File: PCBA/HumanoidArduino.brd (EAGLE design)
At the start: 105.4 x 75.2 mm, 8 parts, among them J1 22-27-2061-06, J2 22-27-2041-04, J3 22-27-2031-03

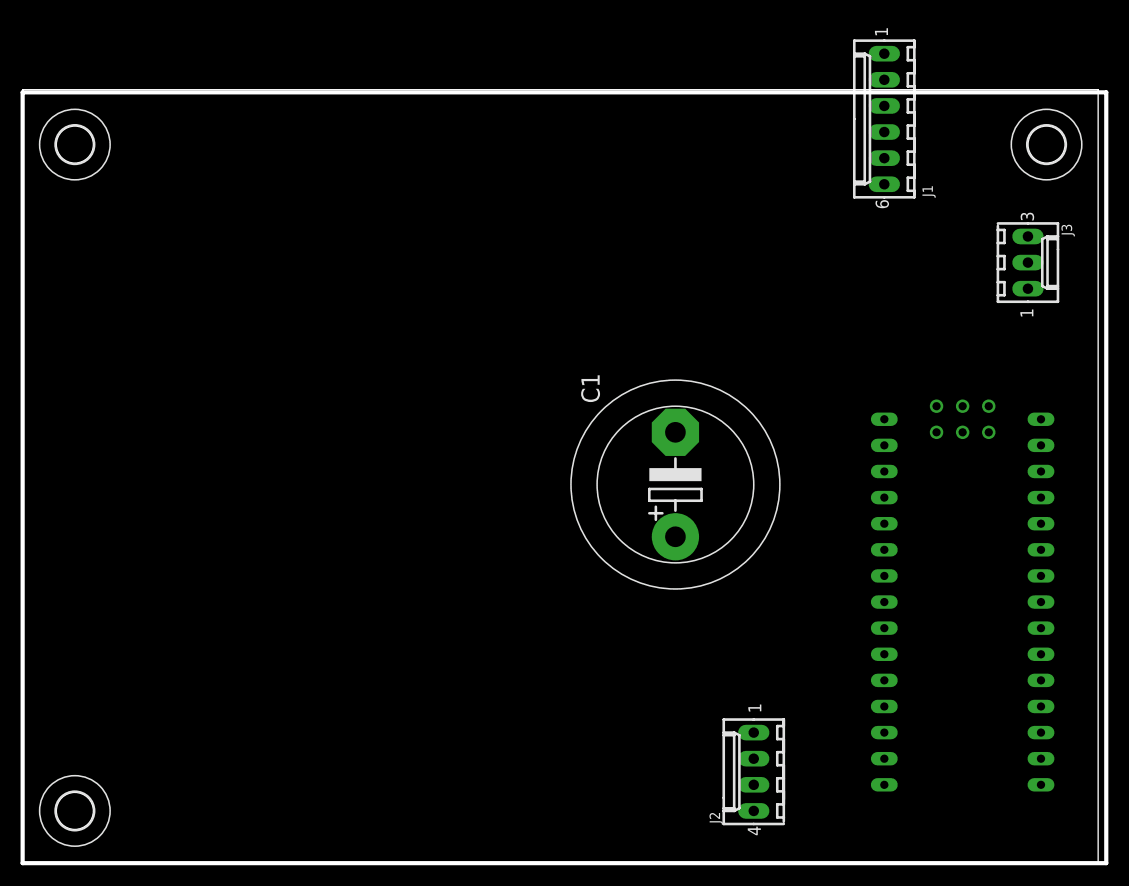
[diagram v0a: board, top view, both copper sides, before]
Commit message: Replaces Arduino w. CHIP
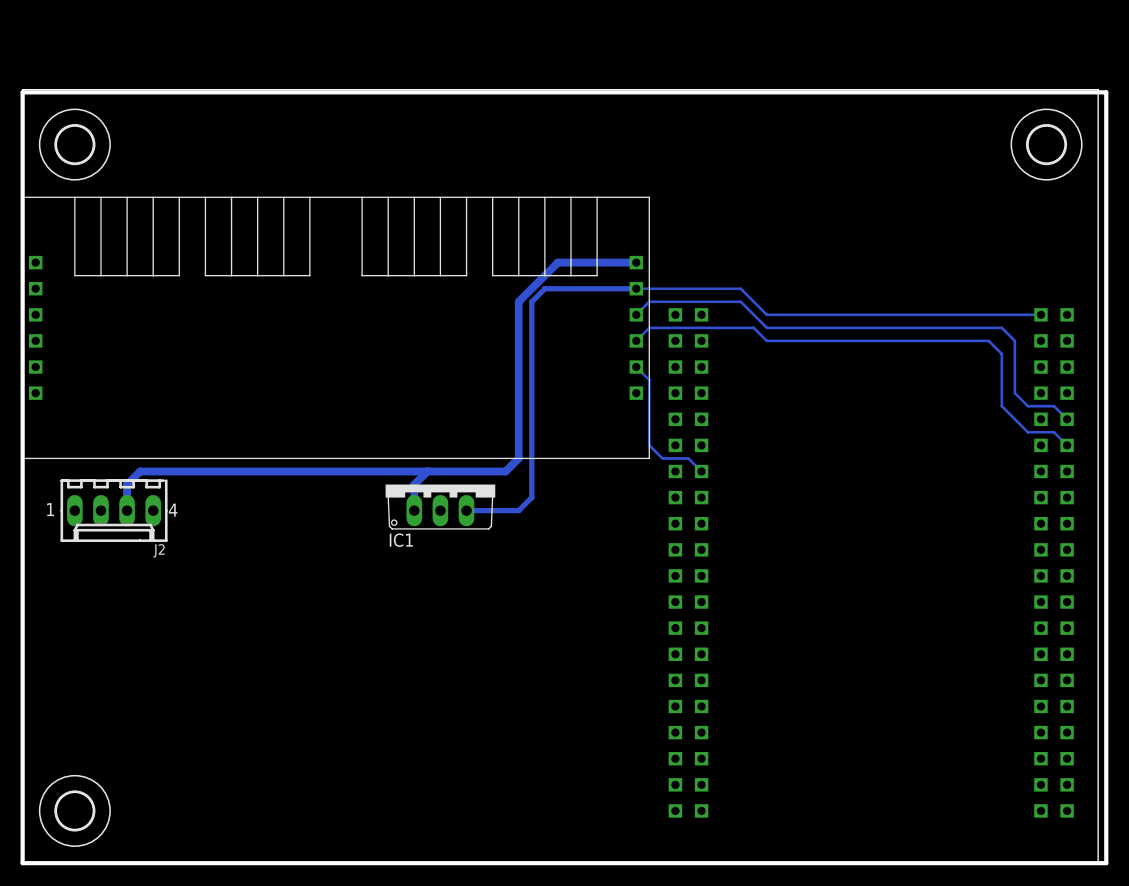
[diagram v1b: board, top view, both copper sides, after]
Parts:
- removed C1: (no value), adafruit:EB20D
- removed J1: 22-27-2061-06, con-molex:6410-06
- removed J3: 22-27-2031-03, con-molex:6410-03
- removed U$1: NANO, Arduino-clone:NANO
- added IC1: 7805TV, linear:TO220V
- added U$2: ADAFRUIT_PCA9685, ZMZE:ADAFRUIT_PCA9685
- added U$3: CHIP, ZMZE:CHIP
- moved J2 67.2 mm to (8.89, 34.3), turned to 180 degrees
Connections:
- removed net 5V: C1.+, J1.5, J3.2, U$1.5V
- removed net DATA: J3.1
- new net +5V: IC1.3, U$2.VCC_IN, U$3.CHG-IN
- net 8.4V: now also IC1.1, U$2.V+_IN; no longer J1.6, U$1.RAW
- net GND: now also IC1.2, U$2.GND_IN, U$3.GND@0, U$3.GND@1, U$3.GND@2, U$3.GND@3, U$3.GND@4, U$3.GND@5, U$3.GND@6, U$3.GND@7, U$3.GND@8; no longer C1.-, J1.1, J3.3, U$1.GND
- net SCL: now also U$2.SCL_IN, U$3.TWI1-SCK; no longer J1.3, U$1.A5
- net SDA: now also U$2.SDA_IN, U$3.TWI1-SDA; no longer J1.4, U$1.A4
- net \O\E: now also U$2.NOE_IN, U$3.XIO-P0; no longer J1.2, U$1.D2
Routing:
- net +5V: track 0.00 -> 77.0 mm
- net 8.4V: track 0.00 -> 74.3 mm
- net SCL: track 0.00 -> 50.1 mm
- net SDA: track 0.00 -> 50.1 mm
- net \O\E: track 0.00 -> 14.3 mm
- added copper zone on layer 16, net GND
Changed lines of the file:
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@@
 <setting verticaltext="up"/>
 </settings>
-<grid distance="0.05" unitdist="inch" unit="inch" style="lines" multiple="2" display="yes" altdistance="1" altunitdist="mm" altunit="mm"/>
+<grid distance="0.05" unitdist="inch" unit="inch" style="lines" multiple="2" display="yes" altdistance="0.025" altunitdist="mm" altunit="mm"/>
 <layers>
 <layer number="1" name="Top" color="4" fill="1" visible="yes" active="yes"/>
@@
 </autorouter>
 <elements>
-<element name="C1" library="adafruit" package="EB20D" value="" x="63.5" y="36.83" rot="R90"/>
-<element name="J1" library="con-molex" package="6410-06" value="22-27-2061-06" x="83.82" y="72.39" rot="R90">
-<attribute name="OC_FARNELL" value="unknown" x="83.82" y="72.39" size="1.778" layer="27" rot="R90" display="off"/>
-<attribute name="OC_NEWARK" value="unknown" x="83.82" y="72.39" size="1.778" layer="27" rot="R90" display="off"/>
-<attribute name="MPN" value="" x="83.82" y="72.39" size="1.778" layer="27" rot="R90" display="off"/>
-<attribute name="MF" value="" x="83.82" y="72.39" size="1.778" layer="27" rot="R90" display="off"/>
-</element>
-<element name="J3" library="con-molex" package="6410-03" value="22-27-2031-03" x="97.79" y="58.42" rot="R270">
-<attribute name="OC_FARNELL" value="unknown" x="97.79" y="58.42" size="1.778" layer="27" rot="R270" display="off"/>
-<attribute name="OC_NEWARK" value="unknown" x="97.79" y="58.42" size="1.778" layer="27" rot="R270" display="off"/>
-<attribute name="MPN" value="" x="97.79" y="58.42" size="1.778" layer="27" rot="R270" display="off"/>
-<attribute name="MF" value="" x="97.79" y="58.42" size="1.778" layer="27" rot="R270" display="off"/>
-</element>
-<element name="U$1" library="Arduino-clone" package="NANO" value="NANO" x="88.9" y="34.29" rot="R180"/>
-<element name="J2" library="con-molex" package="6410-04" value="22-27-2041-04" x="71.12" y="8.89" rot="R90">
-<attribute name="OC_FARNELL" value="unknown" x="71.12" y="8.89" size="1.778" layer="27" rot="R90" display="off"/>
-<attribute name="OC_NEWARK" value="unknown" x="71.12" y="8.89" size="1.778" layer="27" rot="R90" display="off"/>
-<attribute name="MPN" value="" x="71.12" y="8.89" size="1.778" layer="27" rot="R90" display="off"/>
-<attribute name="MF" value="" x="71.12" y="8.89" size="1.778" layer="27" rot="R90" display="off"/>
+<element name="J2" library="con-molex" package="6410-04" value="22-27-2041-04" x="8.89" y="34.29" rot="R180">
+<attribute name="OC_FARNELL" value="unknown" x="8.89" y="34.29" size="1.778" layer="27" rot="R180" display="off"/>
+<attribute name="OC_NEWARK" value="unknown" x="8.89" y="34.29" size="1.778" layer="27" rot="R180" display="off"/>
+<attribute name="MPN" value="" x="8.89" y="34.29" size="1.778" layer="27" rot="R180" display="off"/>
+<attribute name="MF" value="" x="8.89" y="34.29" size="1.778" layer="27" rot="R180" display="off"/>
 </element>
 <element name="H1" library="holes" package="3,6" value="MOUNT-HOLE3.6" x="5.08" y="5.08"/>
 <element name="H2" library="holes" package="3,6" value="MOUNT-HOLE3.6" x="5.08" y="69.9"/>
 <element name="H3" library="holes" package="3,6" value="MOUNT-HOLE3.6" x="99.6" y="69.9"/>
+<element name="U$2" library="ZMZE" package="ADAFRUIT_PCA9685" value="ADAFRUIT_PCA9685" x="59.69" y="63.5" rot="R180"/>
+<element name="U$3" library="ZMZE" package="CHIP" value="CHIP" x="101.6" y="5.08" rot="MR0"/>
+<element name="IC1" library="linear" package="TO220V" value="7805TV" x="40.64" y="36.83"/>
 </elements>
 <signals>
-<signal name="GND">
-<contactref element="J1" pad="1"/>
-<contactref element="J3" pad="3"/>
-<contactref element="C1" pad="-"/>
-<contactref element="U$1" pad="GND"/>
+<signal name="GND" airwireshidden="yes">
+<contactref element="IC1" pad="2"/>
 <contactref element="J2" pad="1"/>
-<wire x1="63.5" y1="41.91" x2="71.12" y2="12.7" width="0" layer="19" extent="1-1"/>
-<wire x1="99.06" y1="40.64" x2="63.5" y2="41.91" width="0" layer="19" extent="1-1"/>
-<wire x1="97.79" y1="60.96" x2="63.5" y2="41.91" width="0" layer="19" extent="1-1"/>
-<wire x1="83.82" y1="78.74" x2="97.79" y2="60.96" width="0" layer="19" extent="1-1"/>
+<contactref element="U$2" pad="GND_IN"/>
+<contactref element="U$3" pad="GND@0"/>
+<contactref element="U$3" pad="GND@1"/>
+<contactref element="U$3" pad="GND@2"/>
+<contactref element="U$3" pad="GND@3"/>
+<contactref element="U$3" pad="GND@4"/>
+<contactref element="U$3" pad="GND@5"/>
+<contactref element="U$3" pad="GND@6"/>
+<contactref element="U$3" pad="GND@7"/>
+<contactref element="U$3" pad="GND@8"/>
+<polygon width="0.4064" layer="16" isolate="0.254" orphans="yes">
+<vertex x="0" y="0"/>
+<vertex x="0" y="74.93"/>
+<vertex x="105.41" y="74.93"/>
+<vertex x="105.41" y="0"/>
+</polygon>
+<wire x1="66.04" y1="53.34" x2="59.69" y2="45.72" width="0" layer="19" extent="1-1"/>
 </signal>
 <signal name="\O\E">
-<contactref element="J1" pad="2"/>
-<contactref element="U$1" pad="D2"/>
-<wire x1="83.82" y1="33.02" x2="83.82" y2="76.2" width="0" layer="19" extent="1-1"/>
+<contactref element="U$2" pad="NOE_IN"/>
+<contactref element="U$3" pad="XIO-P0"/>
+<wire x1="66.04" y1="38.1" x2="64.77" y2="39.37" width="0.254" layer="16"/>
+<wire x1="64.77" y1="39.37" x2="62.23" y2="39.37" width="0.254" layer="16"/>
+<wire x1="62.23" y1="39.37" x2="60.96" y2="40.64" width="0.254" layer="16"/>
+<wire x1="60.96" y1="40.64" x2="60.96" y2="46.99" width="0.254" layer="16"/>
+<wire x1="60.96" y1="46.99" x2="59.69" y2="48.26" width="0.254" layer="16"/>
 </signal>
 <signal name="SCL">
-<contactref element="J1" pad="3"/>
-<contactref element="U$1" pad="A5"/>
-<wire x1="99.06" y1="27.94" x2="83.82" y2="73.66" width="0" layer="19" extent="1-1"/>
+<contactref element="U$2" pad="SCL_IN"/>
+<contactref element="U$3" pad="TWI1-SCK"/>
+<wire x1="97.79" y1="41.91" x2="100.33" y2="41.91" width="0.254" layer="16"/>
+<wire x1="100.33" y1="41.91" x2="101.6" y2="40.64" width="0.254" layer="16"/>
+<wire x1="97.79" y1="41.91" x2="95.25" y2="44.45" width="0.254" layer="16"/>
+<wire x1="95.25" y1="44.45" x2="95.25" y2="49.53" width="0.254" layer="16"/>
+<wire x1="95.25" y1="49.53" x2="93.98" y2="50.8" width="0.254" layer="16"/>
+<wire x1="93.98" y1="50.8" x2="72.39" y2="50.8" width="0.254" layer="16"/>
+<wire x1="72.39" y1="50.8" x2="71.12" y2="52.07" width="0.254" layer="16"/>
+<wire x1="71.12" y1="52.07" x2="60.96" y2="52.07" width="0.254" layer="16"/>
+<wire x1="60.96" y1="52.07" x2="59.69" y2="50.8" width="0.254" layer="16"/>
 </signal>
 <signal name="SDA">
-<contactref element="J1" pad="4"/>
-<contactref element="U$1" pad="A4"/>
-<wire x1="99.06" y1="25.4" x2="83.82" y2="71.12" width="0" layer="19" extent="1-1"/>
-</signal>
-<signal name="5V">
-<contactref element="J1" pad="5"/>
-<contactref element="U$1" pad="5V"/>
-<contactref element="J3" pad="2"/>
-<contactref element="C1" pad="+"/>
-<wire x1="83.82" y1="68.58" x2="97.79" y2="58.42" width="0" layer="19" extent="1-1"/>
-<wire x1="99.06" y1="35.56" x2="97.79" y2="58.42" width="0" layer="19" extent="1-1"/>
-<wire x1="63.5" y1="31.75" x2="99.06" y2="35.56" width="0" layer="19" extent="1-1"/>
+<contactref element="U$2" pad="SDA_IN"/>
+<contactref element="U$3" pad="TWI1-SDA"/>
+<wire x1="100.33" y1="44.45" x2="101.6" y2="43.18" width="0.254" layer="16"/>
+<wire x1="59.69" y1="53.34" x2="60.96" y2="54.61" width="0.254" layer="16"/>
+<wire x1="60.96" y1="54.61" x2="69.85" y2="54.61" width="0.254" layer="16"/>
+<wire x1="69.85" y1="54.61" x2="72.39" y2="52.07" width="0.254" layer="16"/>
+<wire x1="72.39" y1="52.07" x2="95.25" y2="52.07" width="0.254" layer="16"/>
+<wire x1="95.25" y1="52.07" x2="96.52" y2="50.8" width="0.254" layer="16"/>
+<wire x1="96.52" y1="50.8" x2="96.52" y2="45.72" width="0.254" layer="16"/>
+<wire x1="96.52" y1="45.72" x2="97.79" y2="44.45" width="0.254" layer="16"/>
+<wire x1="97.79" y1="44.45" x2="100.33" y2="44.45" width="0.254" layer="16"/>
 </signal>
 <signal name="8.4V">
-<contactref element="U$1" pad="RAW"/>
 <contactref element="J2" pad="3"/>
-<contactref element="J1" pad="6"/>
-<wire x1="99.06" y1="43.18" x2="83.82" y2="66.04" width="0" layer="19" extent="1-1"/>
-<wire x1="71.12" y1="7.62" x2="99.06" y2="43.18" width="0" layer="19" extent="1-1"/>
-</signal>
-<signal name="DATA">
-<contactref element="J3" pad="1"/>
+<contactref element="U$2" pad="V+_IN"/>
+<contactref element="IC1" pad="1"/>
+<wire x1="59.69" y1="58.42" x2="52.07" y2="58.42" width="0.762" layer="16"/>
+<wire x1="52.07" y1="58.42" x2="48.26" y2="54.61" width="0.762" layer="16"/>
+<wire x1="48.26" y1="54.61" x2="48.26" y2="39.37" width="0.762" layer="16"/>
+<wire x1="48.26" y1="39.37" x2="46.99" y2="38.1" width="0.762" layer="16"/>
+<wire x1="46.99" y1="38.1" x2="39.37" y2="38.1" width="0.762" layer="16"/>
+<wire x1="39.37" y1="38.1" x2="38.1" y2="36.83" width="0.762" layer="16"/>
+<wire x1="10.16" y1="34.29" x2="10.16" y2="36.83" width="0.762" layer="16"/>
+<wire x1="10.16" y1="36.83" x2="11.43" y2="38.1" width="0.762" layer="16"/>
+<wire x1="11.43" y1="38.1" x2="39.37" y2="38.1" width="0.762" layer="16"/>
+<wire x1="38.1" y1="36.83" x2="38.1" y2="34.29" width="0.762" layer="16"/>
 </signal>
 <signal name="4.2V">
@@
 <contactref element="J2" pad="4"/>
 </signal>
+<signal name="+5V">
+<contactref element="IC1" pad="3"/>
+<contactref element="U$2" pad="VCC_IN"/>
+<contactref element="U$3" pad="CHG-IN"/>
+<wire x1="43.18" y1="34.29" x2="48.26" y2="34.29" width="0.508" layer="16"/>
+<wire x1="48.26" y1="34.29" x2="49.53" y2="35.56" width="0.508" layer="16"/>
+<wire x1="49.53" y1="35.56" x2="49.53" y2="54.61" width="0.508" layer="16"/>
+<wire x1="49.53" y1="54.61" x2="50.8" y2="55.88" width="0.508" layer="16"/>
+<wire x1="50.8" y1="55.88" x2="59.69" y2="55.88" width="0.508" layer="16"/>
+<wire x1="59.69" y1="55.88" x2="69.85" y2="55.88" width="0.254" layer="16"/>
+<wire x1="69.85" y1="55.88" x2="72.39" y2="53.34" width="0.254" layer="16"/>
+<wire x1="72.39" y1="53.34" x2="99.06" y2="53.34" width="0.254" layer="16"/>
+</signal>
 </signals>
